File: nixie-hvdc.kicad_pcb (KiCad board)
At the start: 2 copper layers, 39 parts, among them J1 PJ-002B, J2 Screw_Terminal_01x02, J3 Conn_01x10_Socket, J4 Screw_Terminal_01x02, Q1 MPSA42, Q10 MPSA42, Q11 IRF740, Q2 MPSA42, Q3 MPSA42, Q4 MPSA42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

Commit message: more
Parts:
- removed the J3 at (51.5, 18.5)
- added J1: Conn_01x11_Pin, Connector_PinHeader_2.54mm:PinHeader_1x11_P2.54mm_Vertical, F.Cu at (178.2, 122.2)
- added Q11: MPSA42, Package_TO_SOT_THT:TO-92, F.Cu at (152.8, 119.2)
- added R11: 2.2k, Resistor_SMD:R_0805_2012Metric_Pad1.20x1.40mm_HandSolder, F.Cu at (173.8, 122.6)
- NX1: value IN-12A -> IN-12BIN-12-DSUB
- R1, R10, R2, R3, R4, R5, R6, R7, R8, R9: value 10k -> 2.2k
- R14: value 10k -> 22k
- moved R1 172.0 mm to (173.8, 120.0), turned to 180 degrees
- moved R2 166.0 mm to (173.8, 107.0), turned to 180 degrees
- moved R4 164.9 mm to (173.8, 109.6), turned to 180 degrees
- moved R6 164.5 mm to (173.8, 112.2), turned to 180 degrees
- moved R8 163.3 mm to (173.8, 114.8), turned to 180 degrees
- moved Q1 162.6 mm to (166.7, 119.2), turned to 180 degrees
- moved R10 162.1 mm to (173.8, 117.4), turned to 180 degrees
- moved R3 161.9 mm to (173.8, 96.5), turned to 180 degrees
- moved R5 161.1 mm to (173.8, 99.2), turned to 180 degrees
- moved R7 159.8 mm to (173.8, 102.0), turned to 180 degrees
- moved R9 158.8 mm to (173.8, 104.5), turned to 180 degrees
- moved Q6 152.2 mm to (159.8, 119.2), turned to 180 degrees
- moved Q2 139.8 mm to (153.7, 104.1), turned to 180 degrees
- moved J2 139.7 mm to (176.7, 76.2), turned to 90 degrees
- moved Q8 139.6 mm to (163.7, 104.0), turned to 180 degrees
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- renumbered D2 to D1, J1 to J2, J2 to J3, Q11 to Q12, R11 to R_SENSE1
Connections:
- NX1 pad LHDP: (no net) -> /NIXIE_DIGIT_LHDP
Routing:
- net +12V: track 0.00 -> 61.9 mm, vias 0 -> 2
- net /180V: track 0.00 -> 57.5 mm
- net Net-(D1-A): track 0.00 -> 26.8 mm
- net Net-(Q12-S): track 0.00 -> 12.0 mm
- net Net-(R13-Pad1): track 0.00 -> 6.91 mm
- net Net-(U1-FB): track 0.00 -> 6.34 mm
- net Net-(Q12-G): track 0.00 -> 5.14 mm
- net Net-(U1-REF): track 0.00 -> 2.20 mm
- added copper zone on F.Cu, net +12V
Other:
- board outline added: 66 x 66 mm

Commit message: nearly done?
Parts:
- moved Q1 38.6 mm to (128.2, 122.6), turned to 0 degrees
- moved Q11 27.3 mm to (126.5, 112.2), turned to 0 degrees
- moved R14 20.1 mm to (128.5, 117.2), turned to 180 degrees
- moved Q4 13.6 mm to (163.5, 102.2)
- moved NX1 13.0 mm to (145.8, 112.2)
- moved Q6 11.9 mm to (163.8, 108.0), turned to -90 degrees
- moved Q10 10.9 mm to (163.3, 122.5)
- moved Q8 10.7 mm to (163.8, 114.7), turned to -90 degrees
- moved Q2 9.94 mm to (148.7, 95.5), turned to -90 degrees
- moved Q3 8.51 mm to (126.5, 105.4), turned to 0 degrees
- moved Q5 1.58 mm to (130.7, 95.5)
- moved Q7 1.58 mm to (136.5, 95.5)
- moved Q9 1.58 mm to (142.5, 95.5)
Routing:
- net GND: track 0.00 -> 100.3 mm, vias 0 -> 162
- net Net-(Q11-B): track 0.00 -> 53.1 mm, vias 0 -> 1
- net Net-(Q3-B): track 0.00 -> 48.1 mm, vias 0 -> 1
- net Net-(Q5-B): track 0.00 -> 46.7 mm, vias 0 -> 1
- net Net-(Q1-B): track 0.00 -> 43.9 mm, vias 0 -> 1
- net Net-(Q7-B): track 0.00 -> 40.6 mm, vias 0 -> 1
- net Net-(Q9-B): track 0.00 -> 32.2 mm, vias 0 -> 1
- net Net-(Q2-B): track 0.00 -> 27.0 mm, vias 0 -> 1
- net /180V: track 57.5 -> 76.7 mm
- net /NIXIE_DIGIT_9: track 0.00 -> 16.8 mm
- net /NIXIE_DIGIT_8: track 0.00 -> 14.2 mm
- net /NIXIE_DIGIT_2: track 0.00 -> 14.1 mm
- net Net-(Q10-B): track 0.00 -> 13.5 mm, vias 0 -> 1
- net Net-(Q4-B): track 0.00 -> 13.0 mm
- net /NIXIE_DIGIT_3: track 0.00 -> 12.8 mm
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- added copper zone on B.Cu, net GND
- added copper zone on F.Cu, net GND
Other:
- board size 66 x 66 mm -> 62.2 x 65 mm
- board text added: "{ "ViaStitching": "0.2", "SWITCHING_STITCHING_VIAS": { "HSpacing": "1", "VSpacing": "1", "HOffset": "0", "VOffset": "0", "Clearance": "0", "Randomize": false } }"
- board text added: "{ "ViaStitching": "0.2", "SWITCHING_STITCHING_VIAS": { "HSpacing": "3", "VSpacing": "3", "HOffset": "0", "VOffset": "0", "Clearance": "0", "Randomize": false } }"
- board text added: "{ "ViaStitching": "0.2", "SWITCHING_STITCHING_VIAS": { "HSpacing": "7", "VSpacing": "7", "HOffset": "0", "VOffset": "0", "Clearance": "0", "Randomize": false } }"
- board text added: "{ "ViaStitching": "0.2", "SWITCHING_STITCHING_VIAS": { "HSpacing": "7", "VSpacing": "7", "HOffset": "0", "VOffset": "0", "Clearance": "3", "Randomize": false } }"
- board text added: "{ "ViaStitching": "0.2", "SWITCHING_STITCHING_VIAS": { "HSpacing": "7", "VSpacing": "7", "HOffset": "0", "VOffset": "0", "Clearance": "5", "Randomize": false } }"
- board text added: "{ "ViaStitching": "0.2", "stitch_zone_0": { "HSpacing": "1", "VSpacing": "1", "HOffset": "0", "VOffset": "0", "Clearance": "0", "Randomize": false } }"
- board text added: "{ "ViaStitching": "0.2", "stitch_zone_0": { "HSpacing": "3", "VSpacing": "3", "HOffset": "0.5", "VOffset": "1", "Clearance": "0", "Randomize": false } }"

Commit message: done i think
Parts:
- added G***: LOGO, LOGO, F.Cu at (124.8, 65.8)
- added G***: LOGO, LOGO, B.Cu at (174.5, 105.5)
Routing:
- net GND: vias 162 -> 77
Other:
- board text added: "0"
- board text added: "1"
- board text added: "12V"
- board text added: "2"
- board text added: "3"
- board text added: "4"
- board text added: "5"
- board text added: "6"
- board text added: "7"
- board text added: "8"
- board text added: "9"
- board text added: "GND"
- board text added: "HV"
- board text added: "JLCJLCJLCJLC"
- board text added: "LHDP"

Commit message: more stuff
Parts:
- added G***: LOGO, LOGO, B.Cu at (124.3, 92.0)

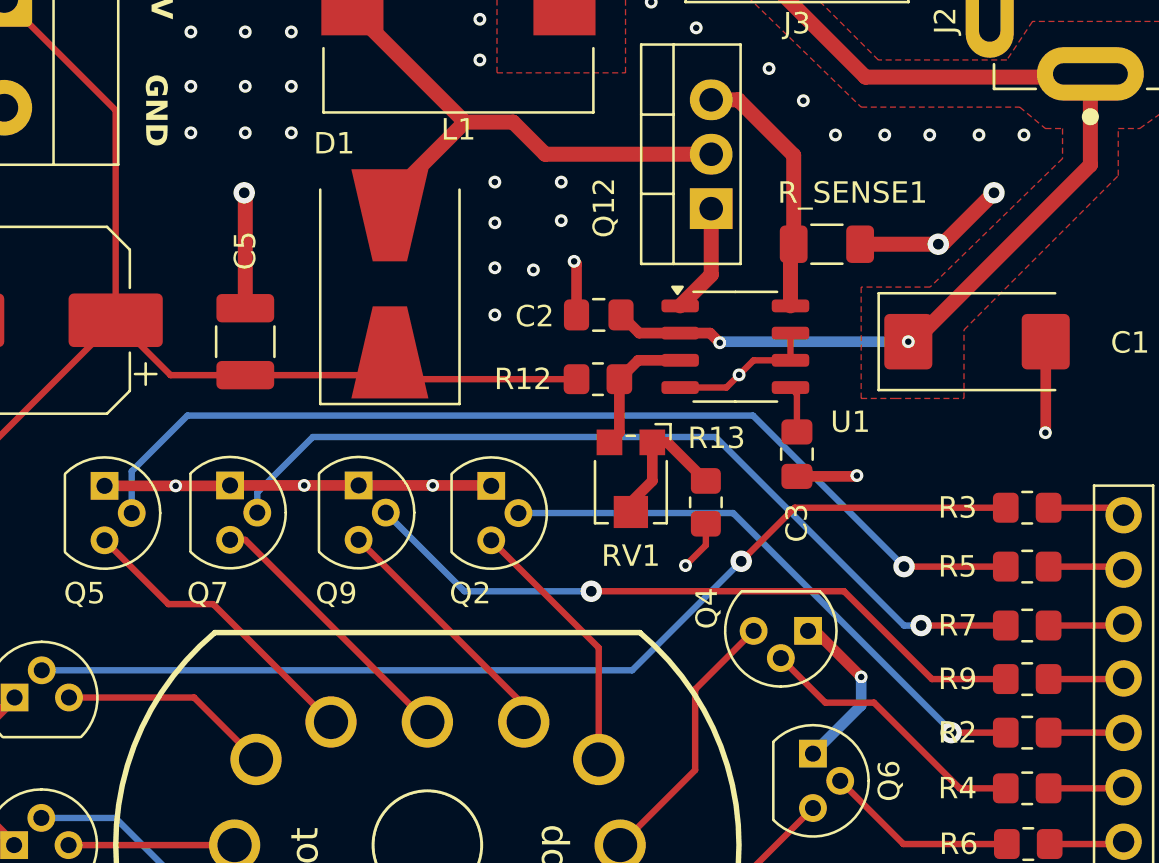
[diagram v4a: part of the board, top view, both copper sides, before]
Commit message: change pot
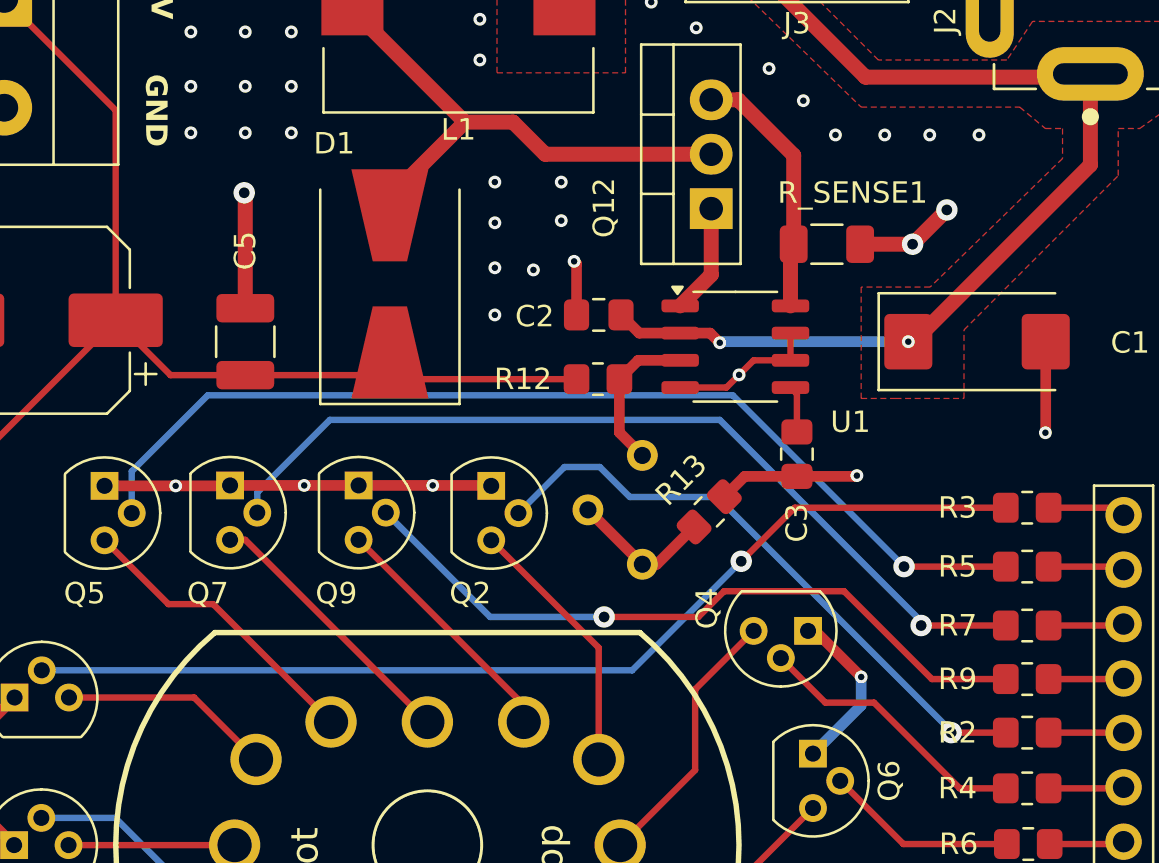
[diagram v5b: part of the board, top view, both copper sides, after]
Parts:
- RV1: value VGF39NCHXT-B502 -> 3386P-1-502LF; footprint Potentiometer_SMD:Potentiometer_Bourns_TC33X_Vertical -> Potentiometer_THT:Potentiometer_Bourns_3386P_Vertical; moved to B.Cu
- moved RV1 3.93 mm to (155.8, 99.1), turned to 180 degrees
- moved R13 0.47 mm to (158.9, 96.7), turned to 45 degrees
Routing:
- net Net-(Q2-B): track 27.0 -> 28.8 mm
- net GND: track 100.3 -> 99.2 mm, vias 77 -> 75
- net Net-(Q9-B): track 32.2 -> 33.2 mm
- net Net-(U1-FB): track 6.34 -> 7.21 mm
- net Net-(Q5-B): track 46.7 -> 47.5 mm
- net Net-(Q7-B): track 40.6 -> 41.4 mm

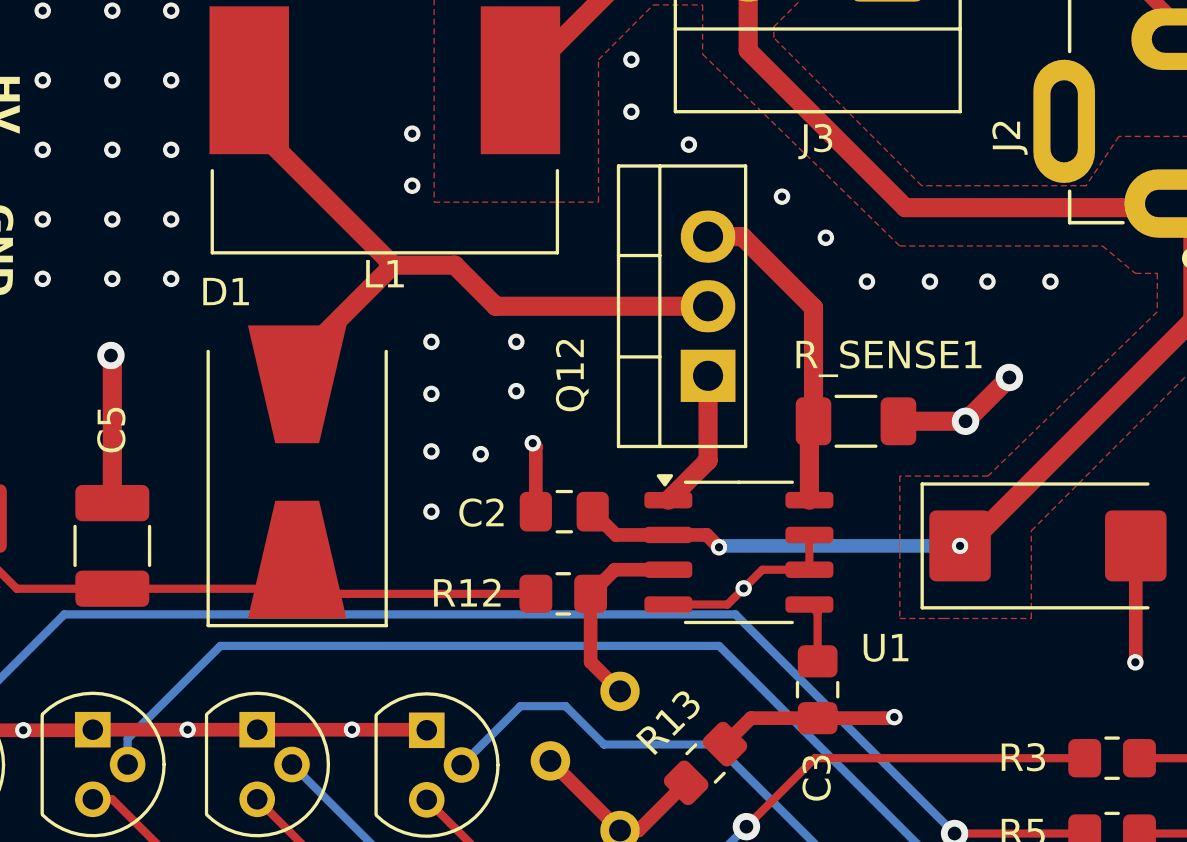
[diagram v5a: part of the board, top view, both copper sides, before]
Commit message: fet orienatiton, r_sense vias
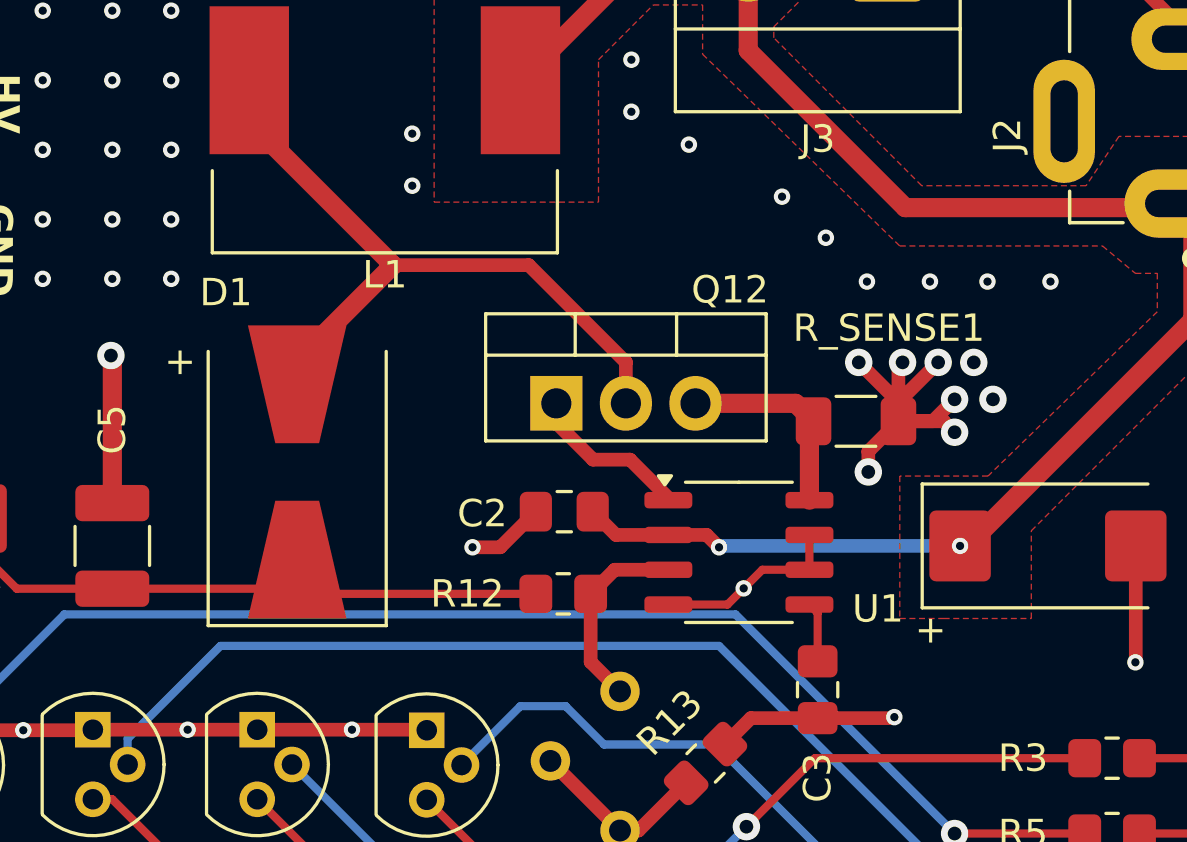
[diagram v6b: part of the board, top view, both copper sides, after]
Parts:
- moved Q12 5.63 mm to (153.5, 83.5), turned to 0 degrees
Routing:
- net GND: track 99.2 -> 109.4 mm, vias 75 -> 74
- net Net-(Q12-S): track 12.0 -> 7.52 mm
- net Net-(Q12-G): track 5.14 -> 5.94 mm
- net Net-(D1-A): track 26.8 -> 26.2 mm
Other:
- board text added: "+"

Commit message: fabbing!
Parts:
- RV1: moved to F.Cu
- moved Q5 9.87 mm to (124.0, 102.8), turned to 0 degrees
- moved Q7 8.96 mm to (127.7, 97.1), turned to 0 degrees
- moved Q2 8.23 mm to (140.5, 95.5)
- moved RV1 7.87 mm to (148.0, 98.0), turned to -90 degrees
- moved Q9 7.79 mm to (134.8, 95.5)
- moved Q1 4.48 mm to (123.8, 122.6)
- moved Q3 4.00 mm to (124.0, 108.5)
- moved Q11 3.02 mm to (124.0, 114.0)
- moved R14 2.61 mm to (126.0, 118.0)
- moved NX1 2.25 mm to (145.8, 114.5)
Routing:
- net GND: track 109.4 -> 86.3 mm, vias 74 -> 98
- net Net-(Q5-B): track 47.5 -> 58.6 mm
- net Net-(Q9-B): track 33.2 -> 42.8 mm
- net /NIXIE_DIGIT_4: track 11.7 -> 21.3 mm
- net /NIXIE_DIGIT_5: track 12.3 -> 20.9 mm
- net /NIXIE_DIGIT_3: track 12.8 -> 21.3 mm
- net Net-(Q2-B): track 28.8 -> 37.0 mm
- net Net-(Q1-B): track 43.9 -> 51.6 mm
- net Net-(Q7-B): track 41.4 -> 48.4 mm
- net Net-(R13-Pad1): track 6.73 -> 12.6 mm
- net Net-(U1-FB): track 7.21 -> 11.4 mm
- net Net-(Q3-B): track 48.1 -> 51.9 mm
- net Net-(Q11-B): track 53.1 -> 56.8 mm
- net /NIXIE_DIGIT_0: track 12.4 -> 15.9 mm
- net /NIXIE_DIGIT_6: track 12.6 -> 15.9 mm
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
